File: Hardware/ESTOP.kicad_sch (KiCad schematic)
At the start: 28 parts, among them J10 Conn_01x02, Q13 SQ2315CES-T1_GE3, Q15 IRLML0030, Q16 IRLML0030, Q17 IRLML0030, Q7 SQ2315CES-T1_GE3, Q8 SQ2315CES-T1_GE3

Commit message: circuit blocks designed, schematic updated
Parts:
- removed Q13, Q7: SQ2315CES-T1_GE3, SQ2315CES-T1_GE3:SOT95P237X112-3N, symbol SQ2315CES-T1_GE3:SQ2315CES-T1_GE3
- removed Q15, Q16, Q17: IRLML0030, Package_TO_SOT_SMD:SOT-23, symbol Transistor_FET:IRLML0030
- removed R63: 470, Resistor_SMD:R_0603_1608Metric, symbol Device:R_US
- removed R88, R89, R90, R92, R96: 10k, Resistor_SMD:R_0603_1608Metric, symbol Device:R_US
- removed R97, R98, R99: 0, Resistor_SMD:R_0603_1608Metric, symbol Device:R_Small_US
- removed TP19, TP20, TP21: TestPoint, TestPoint:TestPoint_Pad_1.0x1.0mm, symbol Connector:TestPoint
- added E_JP1, E_JP2, E_JP3: Jumper_2_Open, Connector_PinHeader_2.54mm:PinHeader_1x02_P2.54mm_Vertical, symbol Jumper:Jumper_2_Open
- added Q15, Q2: SQ2315CES-T1_GE3, SQ2315CES-T1_GE3:SOT95P237X112-3N, symbol SQ2315CES-T1_GE3:SQ2315CES-T1_GE3
- added R35, R5: 33k, Resistor_SMD:R_0603_1608Metric, symbol Device:R_US
- added R71: 470, Resistor_SMD:R_0603_1608Metric, symbol Device:R_US
- R95: value 10k -> 33k
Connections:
- net +24V: now also E_JP1.1 (A)
- net +3.3V: now also Q15.2 (S), Q2.2 (S)
- net ESTOP_1-/2+: now also E_JP1.2 (B), E_JP2.1 (A), R35.2
- net ESTOP_1_SENSE: now also Q15.3 (D), R71.1
- net ESTOP_2-: now also E_JP2.2 (B), E_JP3.1 (A)
- net ESTOP_2_SENSE: now also Q8.3 (D), R69.1; no longer Q8.1 (G)
- net ESTOP_3_SENSE: now also R70.1, Q2.3 (D)
- net ESTOP_OUT: now also E_JP3.2 (B), R5.2
- net at ESTOP1.2 (A): now also R71.2; no longer R70.2
- net at R93.2, R95.1: now also Q8.1 (G)
- net at ESTOP3.2 (A): now also R70.2
- net at R94.2: now also Q2.1 (G), R5.1
- net at R91.2: now also Q15.1 (G), R35.1
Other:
- note added: "Vgs = 10k/(33k+10k)*24V = 5.58V"
- note removed: "Estop Lights"
- note removed: "Vgs ~= 1/2*Vin = 12V"
- moved on the sheet: R91, R93, R94, R95

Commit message: JLC Production Files
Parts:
- added R63, R72, R73: 10k, Resistor_SMD:R_0603_1608Metric, symbol Device:R_US
- ESTOP1, ESTOP2, ESTOP3: LCSC (none) -> C84263
- Q15, Q2, Q8: LCSC (none) -> C10487
- R35, R5, R95: LCSC (none) -> C844778
- R69, R70, R71: LCSC (none) -> C23179
- R91, R93, R94: LCSC (none) -> C25804
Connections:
- net ESTOP_1_SENSE: now also R73.2; no longer Q15.3 (D), R71.1
- net ESTOP_2_SENSE: now also R72.2; no longer Q8.3 (D), R69.1
- net ESTOP_3_SENSE: now also R63.2; no longer Q2.3 (D), R70.1
- new net: Q8.3 (D), R69.1, R72.1
- new net: Q2.3 (D), R63.1, R70.1
- new net: Q15.3 (D), R71.1, R73.1

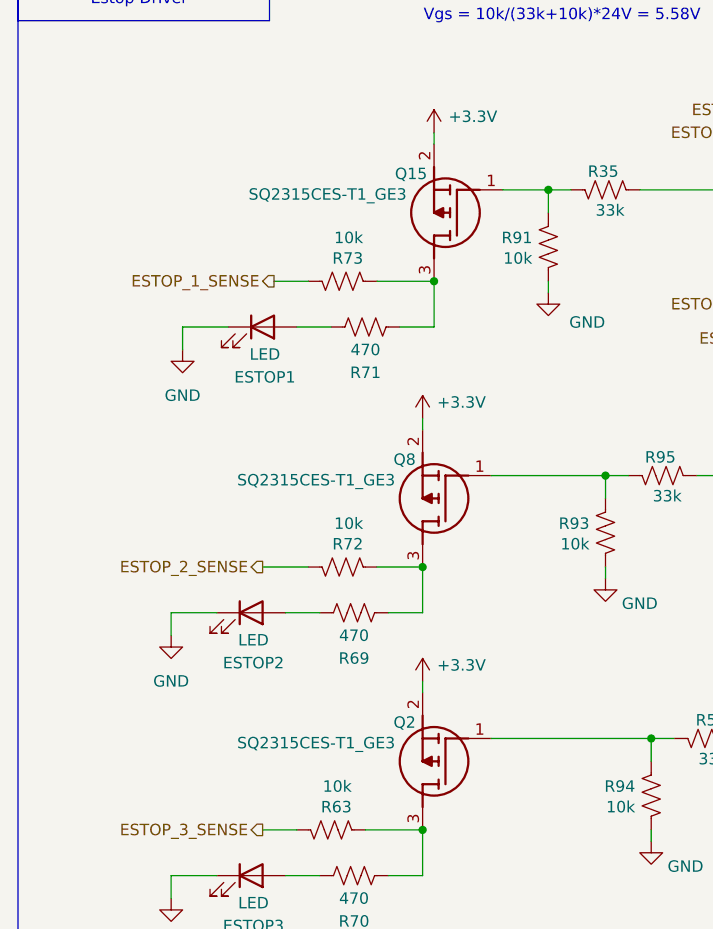
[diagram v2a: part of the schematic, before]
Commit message: condensed custom lirbraries
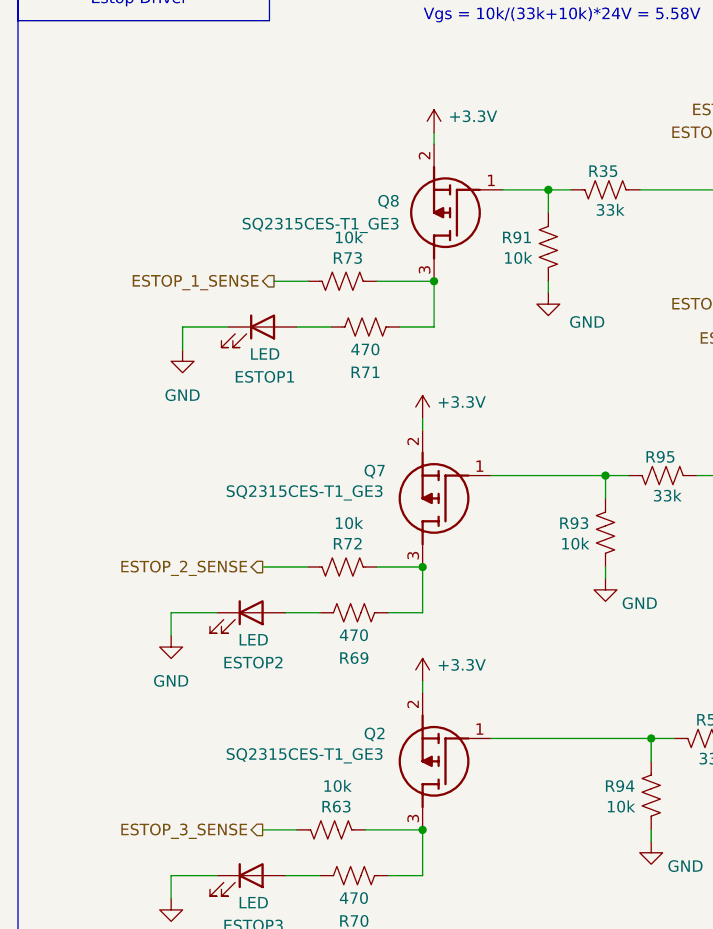
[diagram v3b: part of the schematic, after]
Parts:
- removed Q15, Q2, Q8: SQ2315CES-T1_GE3, SQ2315CES-T1_GE3:SOT95P237X112-3N, symbol SQ2315CES-T1_GE3:SQ2315CES-T1_GE3
- added Q2, Q7, Q8: SQ2315CES-T1_GE3, CustomKiCad-Library:SOT95P237X112-3N, symbol CustomSymbols:SQ2315CES-T1_GE3
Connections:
- net +3.3V: now also Q2.2 (S), Q7.2 (S), Q8.2 (S)
- net at R69.1, R72.1: now also Q7.3 (D)
- net at R5.1, R94.2: now also Q2.1 (G)
- net at R93.2, R95.1: now also Q7.1 (G)
- net at R63.1, R70.1: now also Q2.3 (D)
- net at R71.1, R73.1: now also Q8.3 (D)
- net at R35.1, R91.2: now also Q8.1 (G)

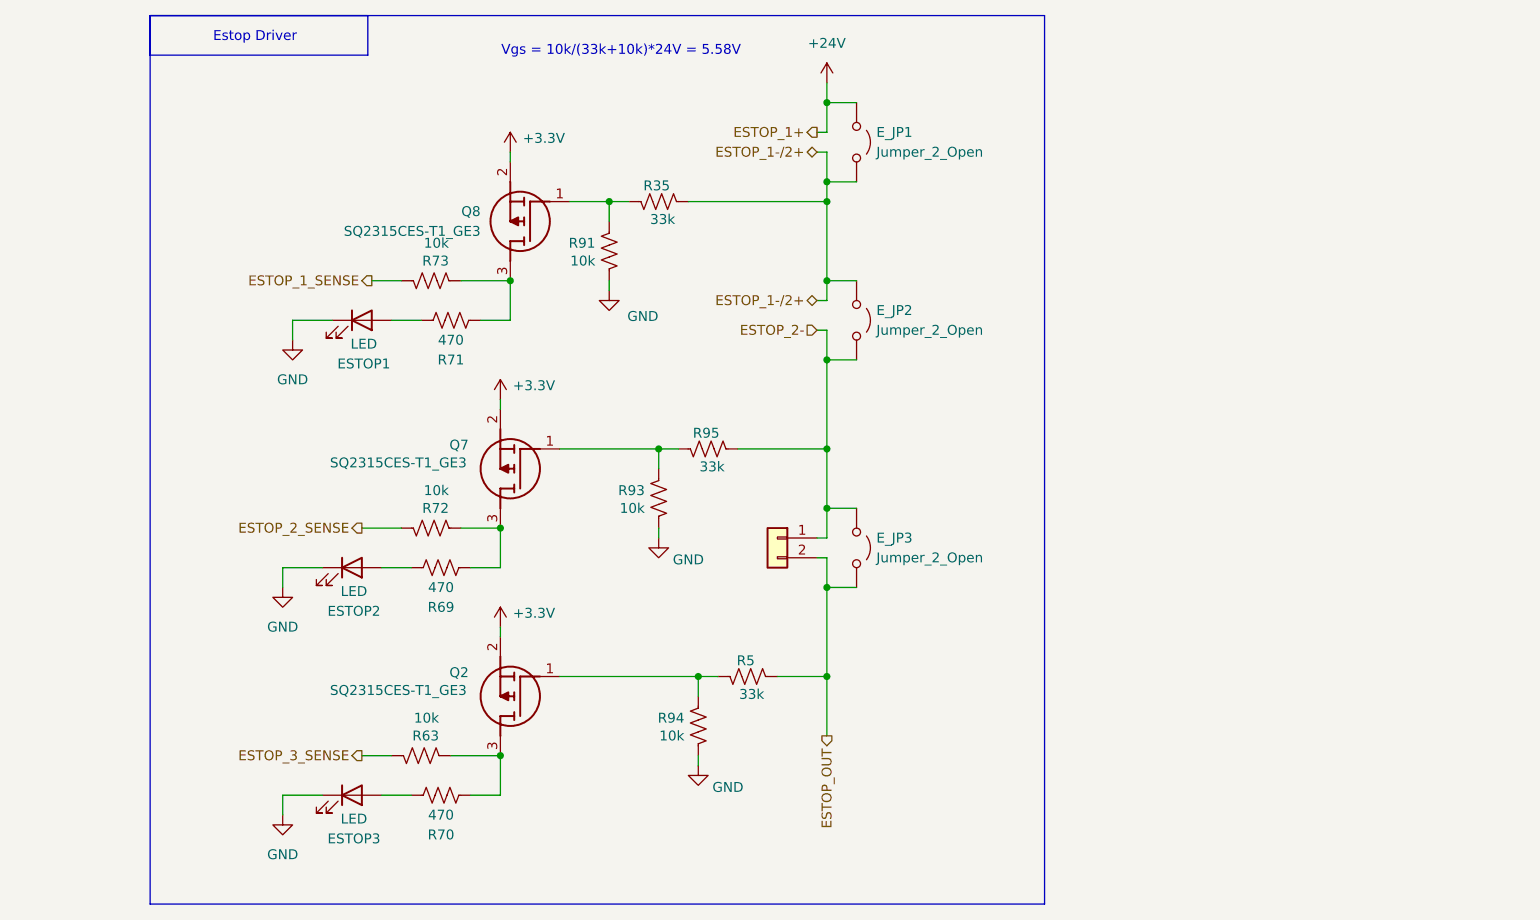
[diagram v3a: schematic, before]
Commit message: added ESTOP sense pulldowns
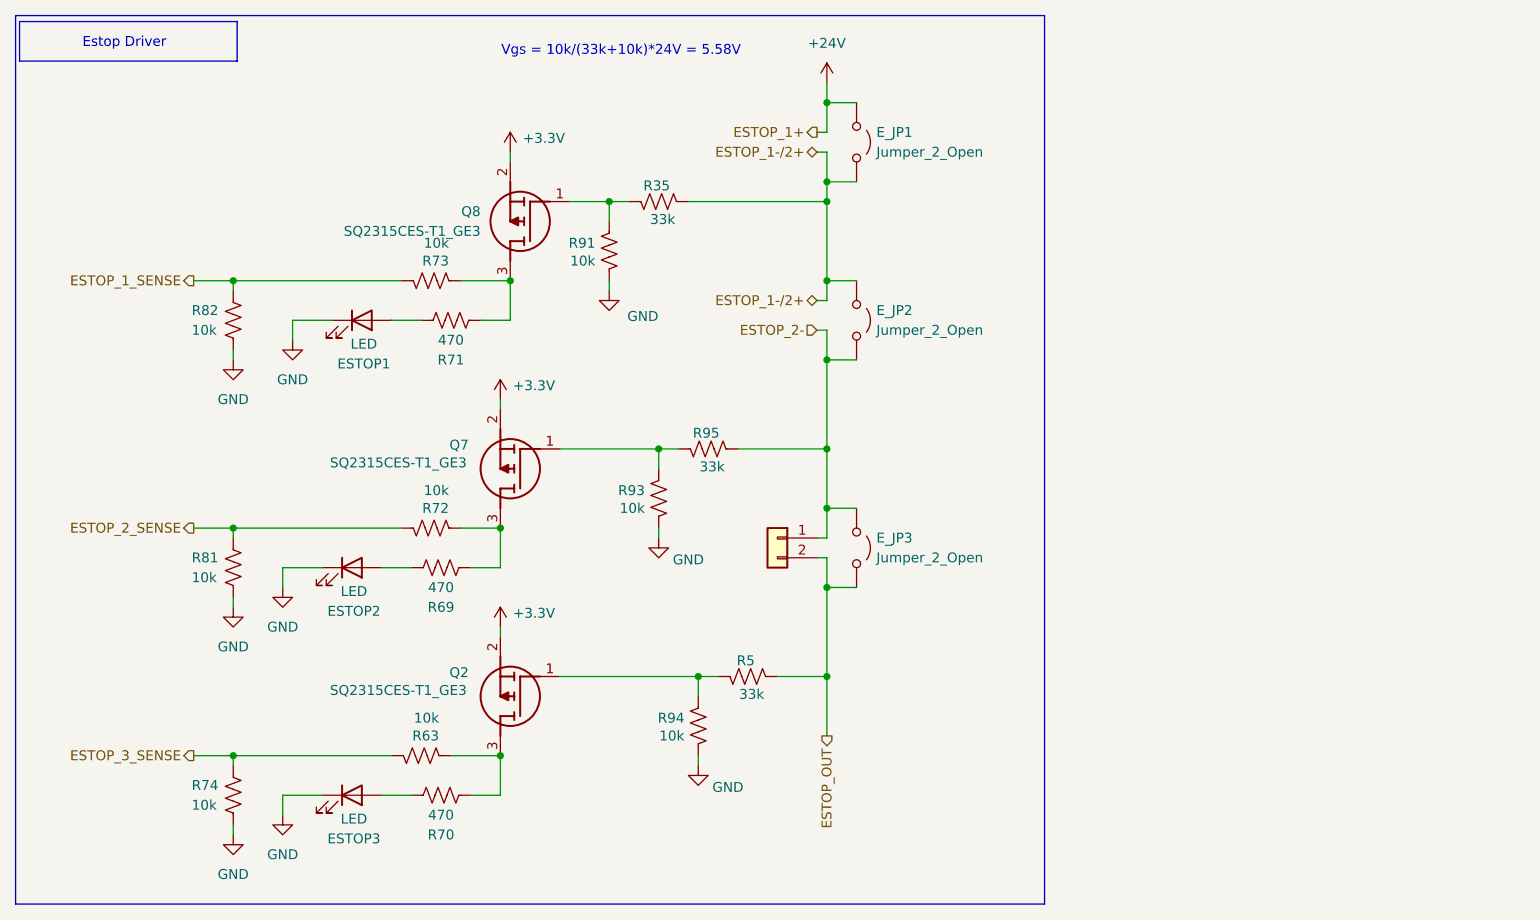
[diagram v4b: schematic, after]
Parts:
- added R74, R81, R82: 10k, Resistor_SMD:R_0603_1608Metric, symbol Device:R_US
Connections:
- net ESTOP_1_SENSE: now also R82.2
- net ESTOP_2_SENSE: now also R81.2
- net ESTOP_3_SENSE: now also R74.2
- net GND: now also R74.1, R81.1, R82.1

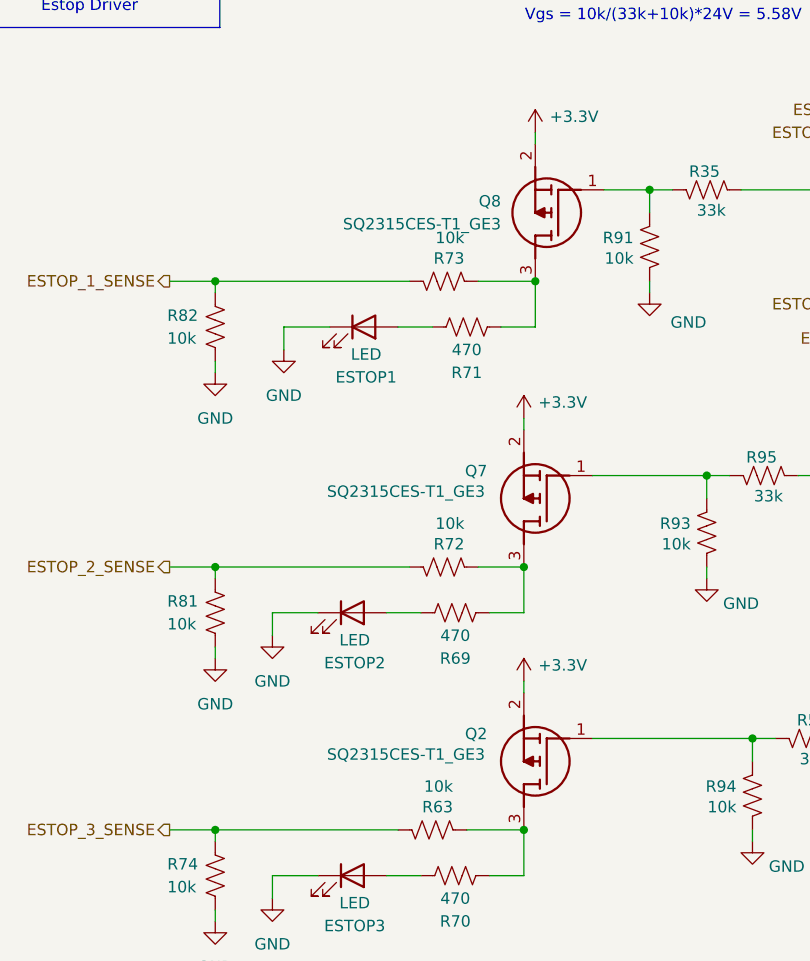
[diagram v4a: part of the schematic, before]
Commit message: removed voltage divider
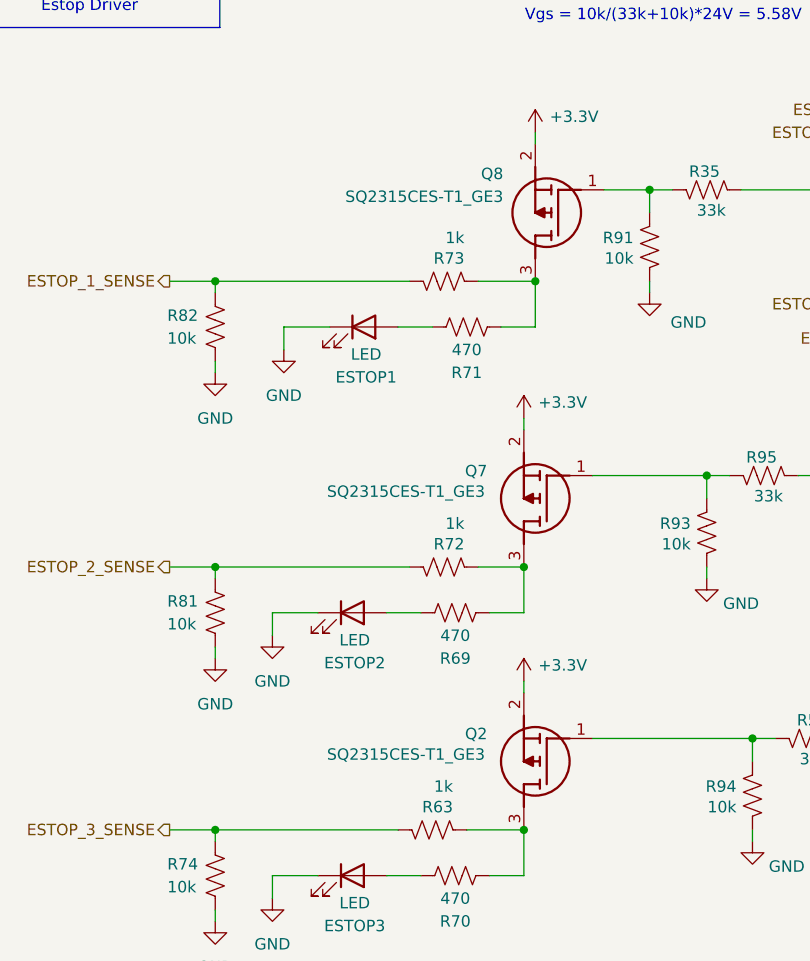
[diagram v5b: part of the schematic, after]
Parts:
- R63, R72, R73: value 10k -> 1k
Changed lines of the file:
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@@
 			)
 		)
-		(property "Value" "10k"
+		(property "Value" "1k"
 			(at 91.186 113.284 90)
 			(effects
@@
 		(on_board yes)
 		(dnp no)
-		(fields_autoplaced yes)
 		(property "Reference" "Q8"
-			(at 95.25 77.4699 0)
+			(at 95.504 74.422 0)
 			(effects
 				(font
@@
 		)
 		(property "Value" "SQ2315CES-T1_GE3"
-			(at 95.25 80.0099 0)
+			(at 95.504 76.962 0)
 			(effects
 				(font
@@
 			)
 		)
-		(property "Value" "10k"
+		(property "Value" "1k"
 			(at 89.916 142.494 90)
 			(effects
@@
 			)
 		)
-		(property "Value" "10k"
+		(property "Value" "1k"
 			(at 91.186 81.534 90)
 			(effects

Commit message: JLCPCB ouput files
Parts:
- R63, R72, R73: P/N CRCW060310K0FKEI -> CRCW06031K00FKEI
- R69, R70, R71: P/N CRCW0603120RFKEC -> CRCW1206470RFKEA
